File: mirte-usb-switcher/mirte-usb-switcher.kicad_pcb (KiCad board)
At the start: 2 copper layers, 18.4 x 27.4 mm, 5 parts, among them J1 Conn_02x02_Counter_Clockwise, U1 SIP32509DT-T1-GE3

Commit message: move usb switcher
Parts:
- removed USB1: U254-051T-4BH83-S1S, lcsc:MICRO-USB-SMD_U254-051T-4BH83-S1S
- added C1: 10uF, Capacitor_SMD:C_0805_2012Metric, F.Cu at (55.0, 79.6)
- added C2: 100nF, Capacitor_SMD:C_0805_2012Metric, F.Cu at (58.1, 79.6)
- added D1: LED, LED_SMD:LED_0805_2012Metric, F.Cu at (57.0, 75.6)
- added D2: LED, LED_SMD:LED_0805_2012Metric, F.Cu at (54.4, 75.7)
- added D3: LED, LED_SMD:LED_0805_2012Metric, F.Cu at (62.0, 75.6)
- added D4: LED, LED_SMD:LED_0805_2012Metric, F.Cu at (59.5, 75.7)
- added J2: Conn_01x04_Pin, Connector_PinHeader_2.54mm:PinHeader_1x04_P2.54mm_Vertical, F.Cu at (54.5, 68.4)
- added J3: USB_B_Micro, Connector_USB:USB_Micro-AB_Molex_47590-0001, F.Cu at (70.1, 76.9)
- added R2: R, Resistor_SMD:R_0805_2012Metric, F.Cu at (57.0, 72.2)
- added R3: R, Resistor_SMD:R_0805_2012Metric, F.Cu at (54.4, 72.2)
- added R4: R, Resistor_SMD:R_0805_2012Metric, F.Cu at (62.0, 72.2)
- added R5: R, Resistor_SMD:R_0805_2012Metric, F.Cu at (59.5, 72.2)
- J1: value Conn_02x02_Counter_Clockwise -> Conn_02x04_Odd_Even; footprint Connector_PinHeader_2.54mm:PinHeader_2x02_P2.54mm_Vertical -> Connector_PinSocket_2.54mm:PinSocket_2x04_P2.54mm_Vertical
- moved J1 10.6 mm to (53.9, 62.1)
- moved USB2 8.43 mm to (61.2, 84.7), turned to 0 degrees
- moved U1 6.96 mm to (66.8, 69.8)
- moved R1 0.97 mm to (66.8, 67.0), turned to 0 degrees
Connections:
- net Net-(USB1-VBUS) renamed /VIN
- net Net-(USB2-VCC) renamed /VOUT
- J1 pad 1: unconnected-(J1-Pin_1-Pad1) -> +5V
- J1 pad 2: unconnected-(J1-Pin_2-Pad2) -> +3V3
- J1 pad 3: GND -> +5V
- J1 pad 4: /SW -> /GPIO4_B4
- R1 pad 1: /SW -> /GPIO4_A4
- U1 pad 3: /SW -> /GPIO4_A4
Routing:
- net GND: track 2.82 -> 39.0 mm, vias 1 -> 7
- net /VOUT: track 4.70 -> 33.3 mm
- net /SW: track 17.5 -> 0.00 mm
- net /GPIO4_A4: track 0.00 -> 16.0 mm
- net /GPIO0_D1: track 0.00 -> 10.2 mm
- net /GPIO4_B4: track 0.00 -> 7.83 mm
- net /GPIO4_B5: track 0.00 -> 7.81 mm
- net +5V: track 0.00 -> 2.54 mm
- net Net-(D2-A): track 0.00 -> 1.63 mm
- net Net-(D3-A): track 0.00 -> 1.58 mm
- net Net-(D4-A): track 0.00 -> 1.58 mm
- net Net-(D1-A): track 0.00 -> 1.57 mm
- net /D-: track 9.36 -> 10.6 mm, vias 1 -> 0
- net /D+: track 8.58 -> 9.11 mm, vias 1 -> 0
- net /VIN: track 8.70 -> 8.91 mm, vias 2 -> 0
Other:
- board size 18.4 x 27.4 mm -> 19 x 33 mm

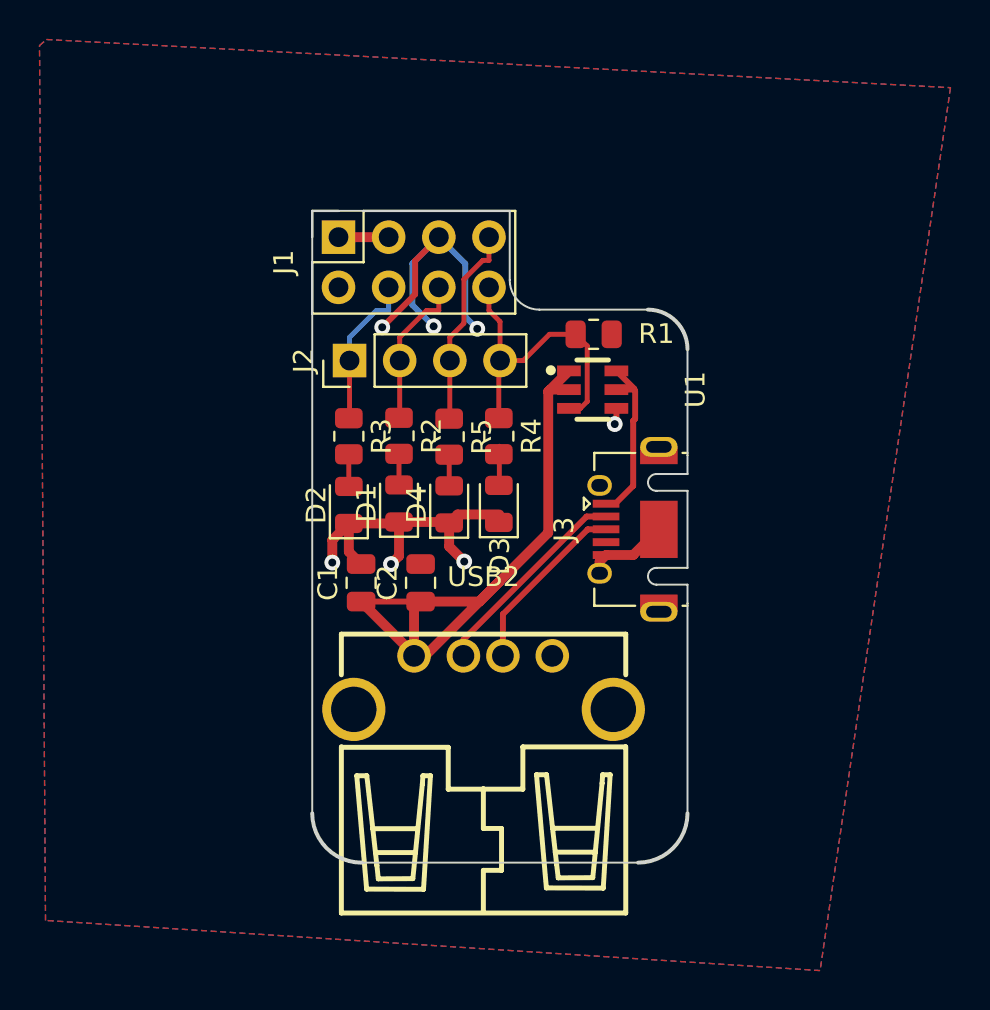
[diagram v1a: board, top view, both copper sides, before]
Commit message: usb switcher done
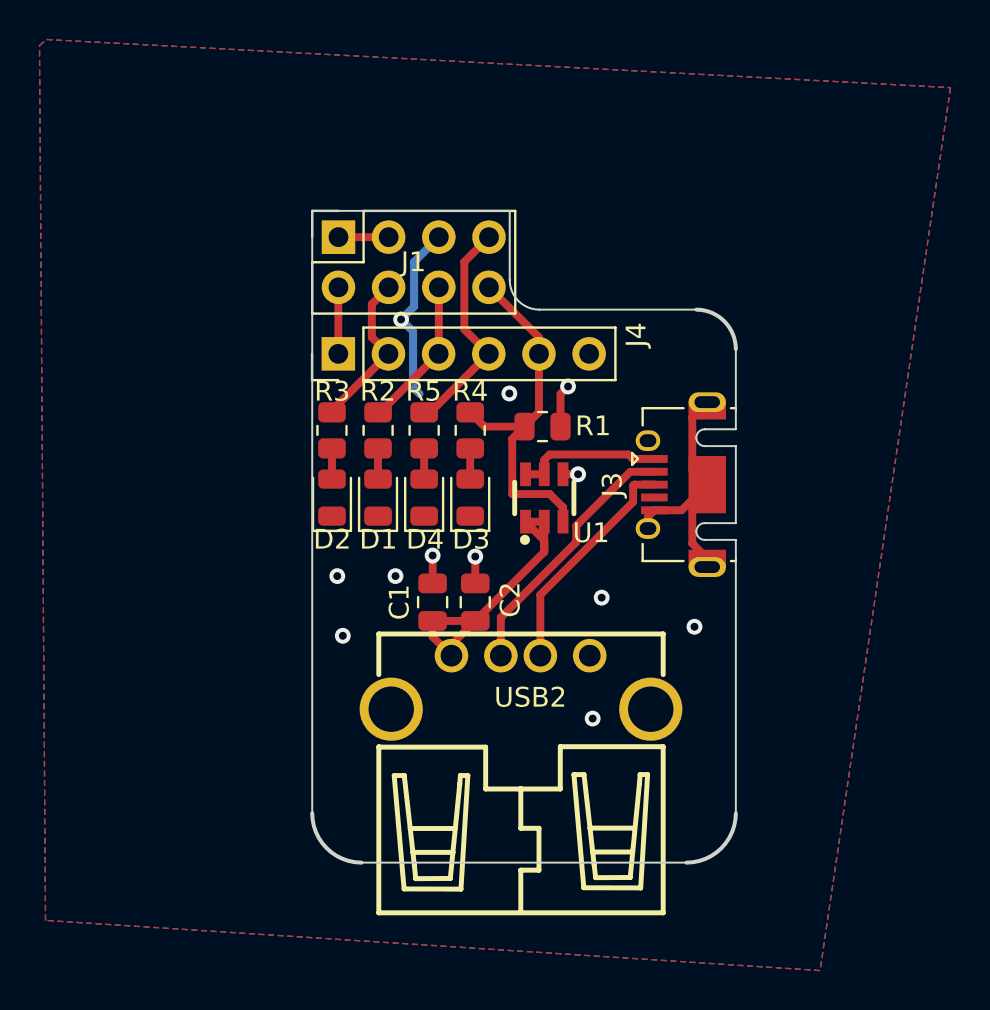
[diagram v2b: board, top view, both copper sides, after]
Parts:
- removed J2: Conn_01x04_Pin, Connector_PinHeader_2.54mm:PinHeader_1x04_P2.54mm_Vertical
- added J4: Conn_01x06_Pin, Connector_PinHeader_2.54mm:PinHeader_1x06_P2.54mm_Vertical, F.Cu at (53.9, 68.0)
- moved U1 6.01 mm to (64.3, 75.3), turned to 0 degrees
- moved R1 5.34 mm to (64.2, 71.7)
- moved C1 3.75 mm to (58.7, 80.6)
- moved J3 3.34 mm to (72.6, 74.7)
- moved C2 2.94 mm to (60.8, 80.6)
- moved USB2 1.90 mm to (63.1, 84.7)
- moved D3 1.48 mm to (60.6, 75.3)
- moved R4 1.48 mm to (60.6, 71.9)
- moved D4 1.31 mm to (58.2, 75.3)
- moved R5 1.31 mm to (58.2, 71.9)
- moved D1 1.10 mm to (55.9, 75.3)
- moved R2 1.10 mm to (55.9, 71.9)
- moved D2 0.93 mm to (53.6, 75.3)
- moved R3 0.90 mm to (53.6, 71.9)
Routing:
- net /VOUT: track 33.3 -> 15.9 mm
- net GND: track 39.0 -> 28.3 mm, vias 7 -> 12
- net +3V3: track 0.00 -> 3.37 mm
- net /GPIO4_A4: track 16.0 -> 18.7 mm
- net /D-: track 10.6 -> 13.2 mm
- net /D+: track 9.11 -> 11.7 mm
- net /VIN: track 8.91 -> 7.46 mm
- net /GPIO0_D1: track 10.2 -> 11.4 mm
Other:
- board size 19 x 33 mm -> 21.4 x 33 mm

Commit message: Fixes lcsc shortage
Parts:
- added G1: LOGO, graphics:tudelft_logo_10mm, F.Cu at (72.3, 87.8)
- R1: value R -> 10k
- R2, R3, R4, R5: value R -> 220
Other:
- board text added: "3V3 GPIO4_B4 GPIO4_B5 GPIO0_D1 GPIO4_A4* GND"
- board text added: "Mirte USB Switch"

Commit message: Final touches before order
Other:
- board text added: "MIRTE USB Switch"
- board text removed: "Mirte USB Switch"
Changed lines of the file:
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@@
   (gr_line locked (start 62.5688 60.7984) (end 62.5688 64.2984)
     (stroke (width 0.1) (type default)) (layer "Edge.Cuts"))
-  (gr_text "Mirte USB Switch" (at 68.266 79.7468) (layer "B.SilkS")
+  (gr_text "MIRTE USB Switch" (at 68.266 79.7468) (layer "B.SilkS")
     (effects (font (size 1 1) (thickness 0.15)) (justify left bottom mirror))
   )

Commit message: Fix errors(wrong gpio, flipped 5v&gnd)
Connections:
- net /GPIO4_A4 renamed /GPIO4_C3
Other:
- board text added: "3V3 GPIO4_B4 GPIO4_B5 GPIO0_D1 GPIO4_C3* GND"
- board text removed: "3V3 GPIO4_B4 GPIO4_B5 GPIO0_D1 GPIO4_A4* GND"
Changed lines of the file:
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@@
   (net 8 "/GPIO4_B4")
   (net 9 "/GPIO4_B5")
-  (net 10 "/GPIO4_A4")
+  (net 10 "/GPIO4_C3")
   (net 11 "+5V")
   (net 12 "/GPIO0_D1")
@@
       (stroke (width 0.1) (type solid)) (layer "F.Fab"))
     (pad "1" smd roundrect locked (at -0.9125 0) (size 1.025 1.4) (layers "F.Cu" "F.Paste" "F.Mask") (roundrect_rratio 0.243902439)
-      (net 10 "/GPIO4_A4") (pintype "passive"))
+      (net 10 "/GPIO4_C3") (pintype "passive"))
     (pad "2" smd roundrect locked (at 0.9125 0) (size 1.025 1.4) (layers "F.Cu" "F.Paste" "F.Mask") (roundrect_rratio 0.243902439)
       (net 3 "GND") (pintype "passive"))
@@
       (net 16 "/VOUT") (pinfunction "OUT") (pintype "unspecified"))
     (pad "3" smd rect locked (at 0.95 1.2) (size 0.55 1.2) (layers "F.Cu" "F.Paste" "F.Mask")
-      (net 10 "/GPIO4_A4") (pinfunction "EN") (pintype "unspecified"))
+      (net 10 "/GPIO4_C3") (pinfunction "EN") (pintype "unspecified"))
     (pad "4" smd rect locked (at 0.95 -1.2) (size 0.55 1.2) (layers "F.Cu" "F.Paste" "F.Mask")
       (net 3 "GND") (pinfunction "GND") (pintype "unspecified"))
@@
       (net 12 "/GPIO0_D1") (pinfunction "Pin_7") (pintype "passive"))
     (pad "8" thru_hole oval locked (at -2.54 7.62 90) (size 1.7 1.7) (drill 1) (layers "*.Cu" "*.Mask")
-      (net 10 "/GPIO4_A4") (pinfunction "Pin_8") (pintype "passive"))
+      (net 10 "/GPIO4_C3") (pinfunction "Pin_8") (pintype "passive"))
     (model "${KICAD6_3DMODEL_DIR}/Connector_PinSocket_2.54mm.3dshapes/PinSocket_2x04_P2.54mm_Vertical.wrl"
       (offset (xyz 0 0 0))
@@
       (stroke (width 0.1) (type solid)) (layer "F.Fab"))
     (pad "1" smd roundrect locked (at -0.9125 0 270) (size 1.025 1.4) (layers "F.Cu" "F.Paste" "F.Mask") (roundrect_rratio 0.243902439)
-      (net 10 "/GPIO4_A4") (pintype "passive"))
+      (net 10 "/GPIO4_C3") (pintype "passive"))
     (pad "2" smd roundrect locked (at 0.9125 0 270) (size 1.025 1.4) (layers "F.Cu" "F.Paste" "F.Mask") (roundrect_rratio 0.243902439)
       (net 6 "Net-(D3-A)") (pintype "passive"))
@@
       (net 12 "/GPIO0_D1") (pinfunction "Pin_4") (pintype "passive"))
     (pad "5" thru_hole oval (at 0 10.16 90) (size 1.7 1.7) (drill 1) (layers "*.Cu" "*.Mask")
-      (net 10 "/GPIO4_A4") (pinfunction "Pin_5") (pintype "passive"))
+      (net 10 "/GPIO4_C3") (pinfunction "Pin_5") (pintype "passive"))
     (pad "6" thru_hole oval (at 0 12.7 90) (size 1.7 1.7) (drill 1) (layers "*.Cu" "*.Mask")
       (net 3 "GND") (pinfunction "Pin_6") (pintype "passive"))
@@
     (effects (font (size 1 1) (thickness 0.15)) (justify left bottom mirror))
   )
-  (gr_text "3V3\nGPIO4_B4\nGPIO4_B5\nGPIO0_D1\nGPIO4_A4*\nGND" (at 67.504 69.4344 90) (layer "B.SilkS")
+  (gr_text "3V3\nGPIO4_B4\nGPIO4_B5\nGPIO0_D1\nGPIO4_C3*\nGND" (at 67.504 69.4344 90) (layer "B.SilkS")
     (effects (font (size 1.55 1) (thickness 0.15)) (justify left bottom mirror))
   )
